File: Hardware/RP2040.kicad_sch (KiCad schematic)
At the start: 1 part, among them U1 RP2040

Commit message: Connect RP2040, STM32, temperature sensor
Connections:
- net SPI0_CS0: now reaches U1.3 (GPIO1)
- net SPI0_SCK: now reaches U1.4 (GPIO2)
- net SPI0_TX: now reaches U1.5 (GPIO3)
- net SPI0_RX: now reaches U1.6 (GPIO4)
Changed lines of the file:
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@@
 	(generator_version "9.0")
 	(paper "A3")
+	(wire
+		(pts
+			(xy 127 76.2) (xy 124.46 76.2)
+		)
+		(stroke
+			(width 0)
+			(type default)
+		)
+	)
+	(wire
+		(pts
+			(xy 127 78.74) (xy 124.46 78.74)
+		)
+		(stroke
+			(width 0)
+			(type default)
+		)
+	)
+	(wire
+		(pts
+			(xy 127 81.28) (xy 124.46 81.28)
+		)
+		(stroke
+			(width 0)
+			(type default)
+		)
+	)
+	(wire
+		(pts
+			(xy 127 73.66) (xy 124.46 73.66)
+		)
+		(stroke
+			(width 0)
+			(type default)
+		)
+	)
+	(hierarchical_label "SPI0_CS0"
+		(shape bidirectional)
+		(at 127 73.66 0)
+		(effects
+			(font
+				(size 1.27 1.27)
+			)
+			(justify left)
+		)
+	)
+	(hierarchical_label "SPI0_SCK"
+		(shape bidirectional)
+		(at 127 76.2 0)
+		(effects
+			(font
+				(size 1.27 1.27)
+			)
+			(justify left)
+		)
+	)
+	(hierarchical_label "SPI0_TX"
+		(shape bidirectional)
+		(at 127 78.74 0)
+		(effects
+			(font
+				(size 1.27 1.27)
+			)
+			(justify left)
+		)
+	)
+	(hierarchical_label "SPI0_RX"
+		(shape bidirectional)
+		(at 127 81.28 0)
+		(effects
+			(font
+				(size 1.27 1.27)
+			)
+			(justify left)
+		)
+	)
 	(symbol
 		(lib_id "MCU_RaspberryPi:RP2040")

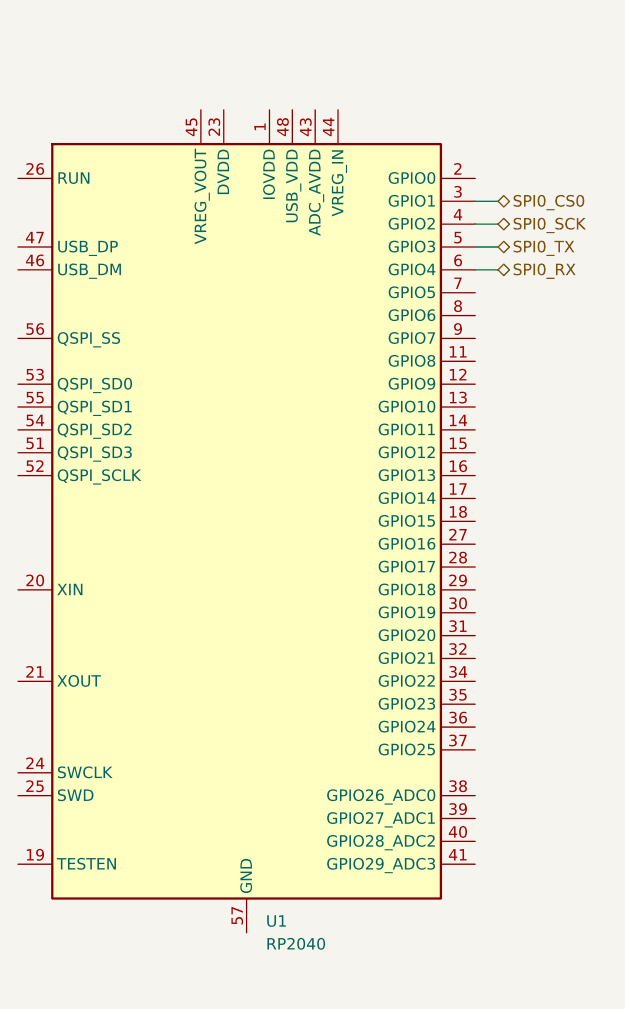
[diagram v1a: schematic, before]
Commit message: Assign SPI1 to Pi 4 <--> STM32
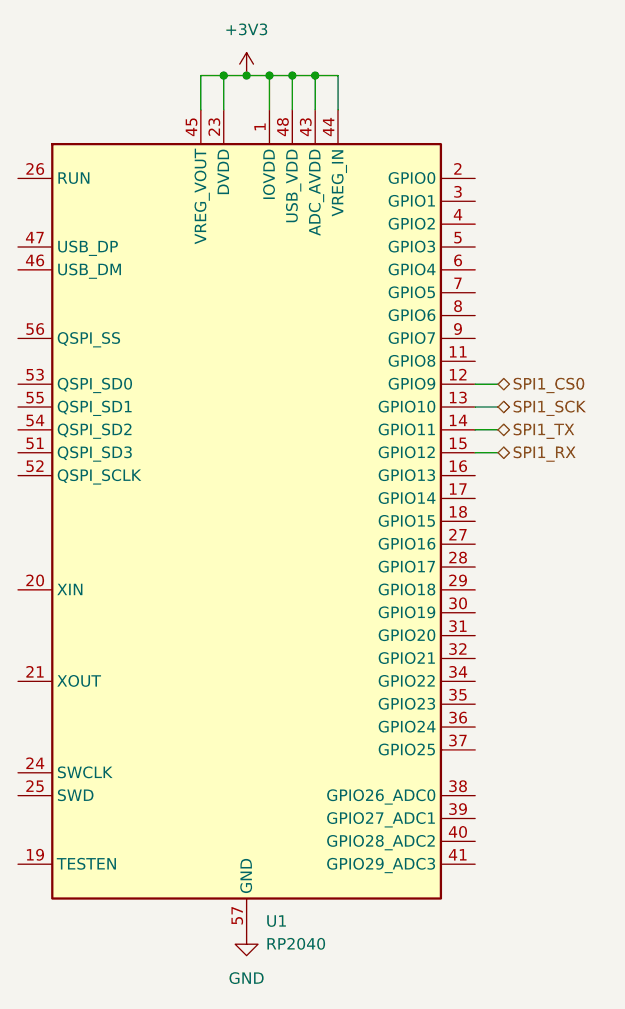
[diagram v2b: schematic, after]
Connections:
- net +3V3: now reaches U1.1 (IOVDD), U1.10 (IOVDD), U1.22 (IOVDD), U1.33 (IOVDD), U1.42 (IOVDD), U1.49 (IOVDD)
- net +3V3: now also U1.23 (DVDD), U1.43 (ADC_AVDD), U1.44 (VREG_IN), U1.45 (VREG_VOUT), U1.48 (USB_VDD), U1.50 (DVDD)
- net SPI1_CS0: now reaches U1.12 (GPIO9)
- net SPI1_SCK: now reaches U1.13 (GPIO10)
- net SPI1_TX: now reaches U1.14 (GPIO11)
- net SPI1_RX: now reaches U1.15 (GPIO12)
- net GND: now reaches U1.57 (GND)
- net SPI0_CS0: no longer names the net of U1.3 (GPIO1)
- net SPI0_RX: no longer names the net of U1.6 (GPIO4)
- net SPI0_SCK: no longer names the net of U1.4 (GPIO2)
- net SPI0_TX: no longer names the net of U1.5 (GPIO3)

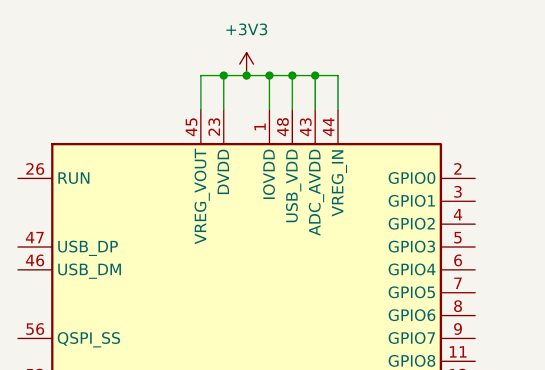
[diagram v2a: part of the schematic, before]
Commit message: Fix RP2040 1V1
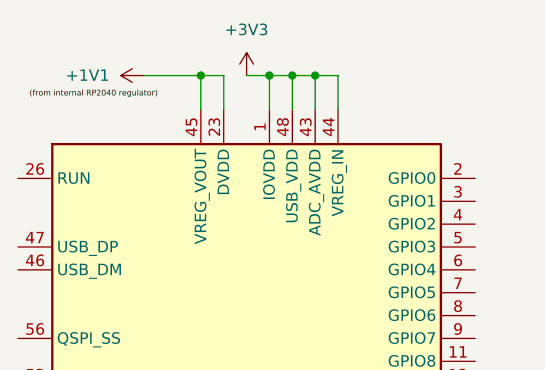
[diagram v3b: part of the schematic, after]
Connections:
- net +3V3: no longer U1.23 (DVDD), U1.45 (VREG_VOUT), U1.50 (DVDD)
- new net +1V1: U1.23 (DVDD), U1.45 (VREG_VOUT), U1.50 (DVDD)
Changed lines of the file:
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@@
 	(paper "A3")
-	(junction
-		(at 99.06 59.69)
-		(diameter 0)
-		(color 0 0 0 0)
-	)
 	(junction
 		(at 101.6 59.69)
@@
 	)
 	(junction
+		(at 93.98 59.69)
+		(diameter 0)
+		(color 0 0 0 0)
+	)
+	(junction
 		(at 104.14 59.69)
 		(diameter 0)
 		(color 0 0 0 0)
 	)
-	(junction
-		(at 96.52 59.69)
-		(diameter 0)
-		(color 0 0 0 0)
-	)
 	(wire
 		(pts
@@
 	(wire
 		(pts
-			(xy 93.98 59.69) (xy 96.52 59.69)
+			(xy 87.63 59.69) (xy 93.98 59.69)
 		)
 		(stroke
@@
 	(wire
 		(pts
-			(xy 96.52 59.69) (xy 96.52 63.5)
-		)
-		(stroke
-			(width 0)
-			(type default)
-		)
-	)
-	(wire
-		(pts
 			(xy 127 99.06) (xy 124.46 99.06)
 		)
@@
 	(wire
 		(pts
-			(xy 96.52 59.69) (xy 99.06 59.69)
-		)
-		(stroke
-			(width 0)
-			(type default)
-		)
-	)
-	(wire
-		(pts
 			(xy 127 101.6) (xy 124.46 101.6)
 		)
@@
 	(wire
 		(pts
+			(xy 96.52 63.5) (xy 96.52 59.69)
+		)
+		(stroke
+			(width 0)
+			(type default)
+		)
+	)
+	(wire
+		(pts
+			(xy 93.98 59.69) (xy 93.98 63.5)
+		)
+		(stroke
+			(width 0)
+			(type default)
+		)
+	)
+	(wire
+		(pts
 			(xy 127 93.98) (xy 124.46 93.98)
 		)
@@
 	(wire
 		(pts
+			(xy 96.52 59.69) (xy 93.98 59.69)
+		)
+		(stroke
+			(width 0)
+			(type default)
+		)
+	)
+	(wire
+		(pts
 			(xy 127 96.52) (xy 124.46 96.52)
 		)
@@
 	(wire
 		(pts
-			(xy 93.98 63.5) (xy 93.98 59.69)
-		)
-		(stroke
-			(width 0)
-			(type default)
-		)
-	)
-	(wire
-		(pts
 			(xy 104.14 59.69) (xy 106.68 59.69)
 		)
@@
 			(width 0)
 			(type default)
+		)
+	)
+	(label "(from internal RP2040 regulator)"
+		(at 74.93 62.23 0)
+		(effects
+			(font
+				(size 0.635 0.635)
+			)
+			(justify left bottom)
 		)
 	)
@@
 					(unit 1)
 				)
+			)
+		)
+	)
+	(symbol
+		(lib_id "power:+3V3")
+		(at 87.63 59.69 90)
+		(unit 1)
+		(exclude_from_sim no)
+		(in_bom yes)
+		(on_board yes)
+		(dnp no)
+		(fields_autoplaced yes)
+		(property "Reference" "#PWR030"
+			(at 91.44 59.69 0)
+			(effects
+				(font
+					(size 1.27 1.27)
+				)
+				(hide yes)
+			)
+		)
+		(property "Value" "+1V1"
+			(at 83.82 59.6899 90)
+			(effects
+				(font
+					(size 1.27 1.27)
+				)
+				(justify left)
+			)
+		)
+		(property "Footprint" ""
+			(at 87.63 59.69 0)
+			(effects
+				(font
+					(size 1.27 1.27)
+				)
+				(hide yes)
+			)
+		)
+		(property "Datasheet" ""
+			(at 87.63 59.69 0)
+			(effects
+				(font
+					(size 1.27 1.27)
+				)
+				(hide yes)
+			)
+		)
+		(property "Description" "Power symbol creates a global label with name \"+3V3\""
+			(at 87.63 59.69 0)
+			(effects
+				(font
+					(size 1.27 1.27)
+				)
+				(hide yes)
+			)
+		)
+		(pin "1"
+		)
+		(instances
+			(project "CTS-SAT-2-OBC-PCB"
+				(path "/58243925-df8d-4fc1-899e-fce866d1d25a/bec95c26-e44f-4f6a-97be-aee51e3bba5a"
+					(reference "#PWR030")
+					(unit 1)
+				)

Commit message: RP2040 Schematic
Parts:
- removed U1: RP2040, Package_DFN_QFN:QFN-56-1EP_7x7mm_P0.4mm_EP3.2x3.2mm, symbol MCU_RaspberryPi:RP2040
- added C1, C10, C11, C12, C13, C14, C4, C5, C7, C9: 100n, Capacitor_SMD:C_0402_1005Metric, symbol Device:C
- added C2, C3: 15p, Capacitor_SMD:C_0402_1005Metric, symbol Device:C
- added C6, C8: 1u, Capacitor_SMD:C_0402_1005Metric, symbol Device:C
- added R1: NP, Resistor_SMD:R_0402_1005Metric, symbol Device:R_US
- added R2, R3: 1k, Resistor_SMD:R_0402_1005Metric, symbol Device:R_US
- added R4, R5: 27, Resistor_SMD:R_0402_1005Metric, symbol Device:R_US
- added U1: W25Q128JVS, Package_SO:SOIC-8_5.23x5.23mm_P1.27mm, symbol Memory_Flash:W25Q128JVS
- added U2: RP2040, RP2040:RP2040-QFN-56, symbol RP2040:RP2040
- added Y1: ABM8-272-T3, Crystal:Crystal_SMD_3225-4Pin_3.2x2.5mm, symbol Device:Crystal_GND24
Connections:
- net +1V1: now also C4.1, C5.1, C6.1, U2.23 (DVDD), U2.45 (VREG_VOUT), U2.50 (DVDD)
- net +3V3: now also C1.1, C10.1, C11.1, C12.1, C13.1, C14.1, C7.1, C8.1, C9.1, R1.2, U1.8 (VCC), U2.1 (IOVDD), U2.10 (IOVDD), U2.22 (IOVDD), U2.33 (IOVDD), U2.42 (IOVDD), U2.43 (ADC_AVDD), U2.44 (VREG_IN), U2.48 (USB_VDD), U2.49 (IOVDD)
- net GND: now also C1.2, C10.2, C11.2, C12.2, C13.2, C14.2, C2.2, C3.2, C4.2, C5.2, C6.2, C7.2, C8.2, C9.2, U1.4 (GND), U2.19 (TESTEN), U2.57 (GND), Y1.2, Y1.4
- net SPI1_CS0: now also U2.12 (GPIO9)
- net SPI1_RX: now also U2.15 (GPIO12)
- net SPI1_SCK: now also U2.13 (GPIO10)
- net SPI1_TX: now also U2.14 (GPIO11)
- new net: C2.1, U2.20 (XIN), Y1.1
- new net: R3.1, U2.21 (XOUT)
- new net: R5.2, U2.46 (USB_DM)
- new net: R4.2, U2.47 (USB_DP)
- new net: U1.7 (IO3), U2.51 (QSPI_SD3)
- new net: U1.6 (CLK), U2.52 (QSPI_SCLK)
- new net: U1.5 (DI(IO0)), U2.53 (QSPI_SD0)
- new net: U1.3 (IO2), U2.54 (QSPI_SD2)
- new net: U1.2 (DO(IO1)), U2.55 (QSPI_SD1)
- new net: R1.1, R2.1, U1.1 (~{CS}), U2.56 (QSPI_SS)
- new net: C3.1, R3.2, Y1.3
- new net RUN: U2.26 (RUN)
- new net SWCLK: U2.24 (SWCLK)
- new net SWD: U2.25 (SWD)
- new net USB_D+: R4.1
- new net USB_D-: R5.1
- new net ~{BOOTSEL}: R2.2
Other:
- note added: "(from internal RP2040 regulator)"
- note added: "Crystal"
- note added: "Flash"
- note added: "Make sure C6 is close to pin 45 of RP2040"
- note added: "Make sure C8 is close to pin 44 of RP2040"
- note added: "Make sure R4 and R5 are close to RP2040"
- note added: "Some other chips may need R1 = 10k"

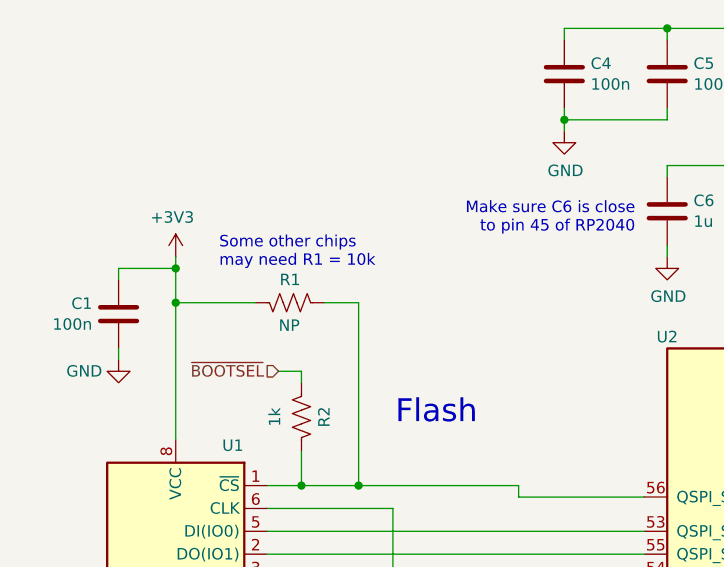
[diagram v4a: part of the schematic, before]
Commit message: Add fast clock
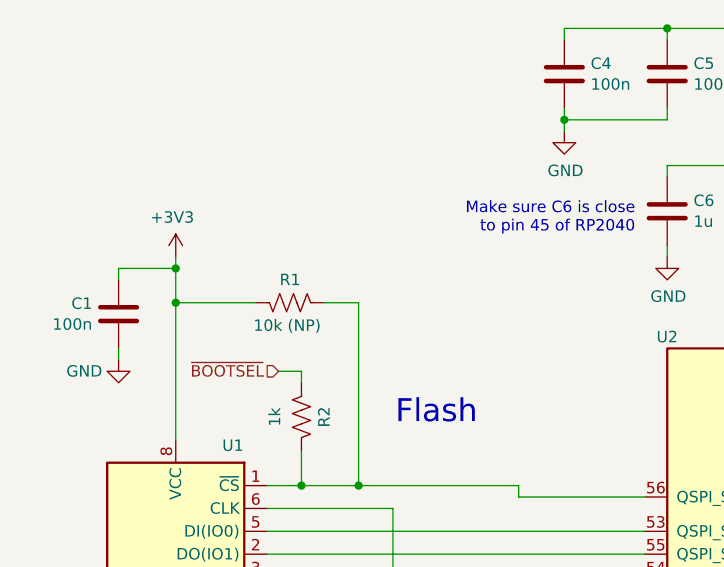
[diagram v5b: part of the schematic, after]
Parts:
- R1: value NP -> 10k (NP)
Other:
- note removed: "Some other chips may need R1 = 10k"
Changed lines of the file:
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@@
 		)
 	)
-	(text "Some other chips \nmay need R1 = 10k"
-		(exclude_from_sim no)
-		(at 128.016 88.9 0)
-		(effects
-			(font
-				(size 1.27 1.27)
-			)
-			(justify left bottom)
-		)
-	)
 	(text "(from internal RP2040 regulator)"
 		(exclude_from_sim no)
@@
 			)
 		)
-		(property "Value" "NP"
-			(at 134.62 95.25 90)
+		(property "Value" "10k (NP)"
+			(at 131.826 95.25 90)
 			(effects
 				(font

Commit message: Connect connectors
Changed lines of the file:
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@@
 		(on_board yes)
 		(dnp no)
-		(property "Reference" "#PWR06"
+		(property "Reference" "#PWR6"
 			(at 123.19 154.94 0)
 			(effects
@@
 		)
 		(property "Value" "GND"
-			(at 119.38 149.86 0)
+			(at 123.19 152.4 0)
 			(effects
 				(font
@@
 			)
 		)
-		(property "Description" ""
+		(property "Description" "Power symbol creates a global label with name \"GND\" , ground"
 			(at 123.19 148.59 0)
 			(effects
@@
 					(size 1.27 1.27)
 				)
-			)
-		)
-		(pin "1"
-		)
-		(instances
-			(project "CTS-SAT-2-OBC-PCB"
-				(path "/58243925-df8d-4fc1-899e-fce866d1d25a/bec95c26-e44f-4f6a-97be-aee51e3bba5a"
-					(reference "#PWR06")
+				(hide yes)
+			)
+		)
+		(pin "1"
+		)
+		(instances
+			(project "CTS-SAT-2-OBC-PCB"
+				(path "/58243925-df8d-4fc1-899e-fce866d1d25a/bec95c26-e44f-4f6a-97be-aee51e3bba5a"
+					(reference "#PWR6")
 					(unit 1)
 				)
@@
 		(on_board yes)
 		(dnp no)
-		(property "Reference" "#PWR012"
+		(property "Reference" "#PWR12"
 			(at 207.01 205.74 0)
 			(effects
@@
 		)
 		(property "Value" "GND"
-			(at 207.137 203.7842 0)
+			(at 207.01 203.2 0)
 			(effects
 				(font
@@
 			)
 		)
-		(property "Description" ""
+		(property "Description" "Power symbol creates a global label with name \"GND\" , ground"
 			(at 207.01 199.39 0)
 			(effects
@@
 					(size 1.27 1.27)
 				)
-			)
-		)
-		(pin "1"
-		)
-		(instances
-			(project "CTS-SAT-2-OBC-PCB"
-				(path "/58243925-df8d-4fc1-899e-fce866d1d25a/bec95c26-e44f-4f6a-97be-aee51e3bba5a"
-					(reference "#PWR012")
+				(hide yes)
+			)
+		)
+		(pin "1"
+		)
+		(instances
+			(project "CTS-SAT-2-OBC-PCB"
+				(path "/58243925-df8d-4fc1-899e-fce866d1d25a/bec95c26-e44f-4f6a-97be-aee51e3bba5a"
+					(reference "#PWR12")
 					(unit 1)
 				)
@@
 		(on_board yes)
 		(dnp no)
-		(property "Reference" "#PWR01"
+		(property "Reference" "#PWR1"
 			(at 116.84 105.41 0)
 			(effects
@@
 		)
 		(property "Value" "GND"
-			(at 113.03 100.33 0)
+			(at 116.84 102.87 0)
 			(effects
 				(font
@@
 			)
 		)
-		(property "Description" ""
+		(property "Description" "Power symbol creates a global label with name \"GND\" , ground"
 			(at 116.84 99.06 0)
 			(effects
@@
 					(size 1.27 1.27)
 				)
-			)
-		)
-		(pin "1"
-		)
-		(instances
-			(project "CTS-SAT-2-OBC-PCB"
-				(path "/58243925-df8d-4fc1-899e-fce866d1d25a/bec95c26-e44f-4f6a-97be-aee51e3bba5a"
-					(reference "#PWR01")
+				(hide yes)
+			)
+		)
+		(pin "1"
+		)
+		(instances
+			(project "CTS-SAT-2-OBC-PCB"
+				(path "/58243925-df8d-4fc1-899e-fce866d1d25a/bec95c26-e44f-4f6a-97be-aee51e3bba5a"
+					(reference "#PWR1")
 					(unit 1)
 				)
@@
 		(on_board yes)
 		(dnp no)
-		(property "Reference" "#PWR015"
+		(property "Reference" "#PWR15"
 			(at 300.99 81.28 0)
 			(effects
@@
 		)
 		(property "Value" "GND"
-			(at 301.117 79.3242 0)
+			(at 300.99 78.74 0)
 			(effects
 				(font
@@
 			)
 		)
-		(property "Description" ""
+		(property "Description" "Power symbol creates a global label with name \"GND\" , ground"
 			(at 300.99 74.93 0)
 			(effects
@@
 					(size 1.27 1.27)
 				)
-			)
-		)
-		(pin "1"
-		)
-		(instances
-			(project "CTS-SAT-2-OBC-PCB"
-				(path "/58243925-df8d-4fc1-899e-fce866d1d25a/bec95c26-e44f-4f6a-97be-aee51e3bba5a"
-					(reference "#PWR015")
+				(hide yes)
+			)
+		)
+		(pin "1"
+		)
+		(instances
+			(project "CTS-SAT-2-OBC-PCB"
+				(path "/58243925-df8d-4fc1-899e-fce866d1d25a/bec95c26-e44f-4f6a-97be-aee51e3bba5a"
+					(reference "#PWR15")
 					(unit 1)
 				)
@@
 		(on_board yes)
 		(dnp no)
-		(property "Reference" "#PWR07"
+		(property "Reference" "#PWR7"
 			(at 135.89 154.94 0)
 			(effects
@@
 		)
 		(property "Value" "GND"
-			(at 139.7 149.86 0)
+			(at 135.89 152.4 0)
 			(effects
 				(font
@@
 			)
 		)
-		(property "Description" ""
+		(property "Description" "Power symbol creates a global label with name \"GND\" , ground"
 			(at 135.89 148.59 0)
 			(effects
@@
 					(size 1.27 1.27)
 				)
-			)
-		)
-		(pin "1"
-		)
-		(instances
-			(project "CTS-SAT-2-OBC-PCB"
-				(path "/58243925-df8d-4fc1-899e-fce866d1d25a/bec95c26-e44f-4f6a-97be-aee51e3bba5a"
-					(reference "#PWR07")
+				(hide yes)
+			)
+		)
+		(pin "1"
+		)
+		(instances
+			(project "CTS-SAT-2-OBC-PCB"
+				(path "/58243925-df8d-4fc1-899e-fce866d1d25a/bec95c26-e44f-4f6a-97be-aee51e3bba5a"
+					(reference "#PWR7")
 					(unit 1)
 				)
@@
 		(on_board yes)
 		(dnp no)
-		(property "Reference" "#PWR011"
+		(property "Reference" "#PWR11"
 			(at 194.31 205.74 0)
 			(effects
@@
 		)
 		(property "Value" "GND"
-			(at 194.437 203.7842 0)
+			(at 194.31 203.2 0)
 			(effects
 				(font
@@
 			)
 		)
-		(property "Description" ""
+		(property "Description" "Power symbol creates a global label with name \"GND\" , ground"
 			(at 194.31 199.39 0)
 			(effects
@@
 					(size 1.27 1.27)
 				)
-			)
-		)
-		(pin "1"
-		)
-		(instances
-			(project "CTS-SAT-2-OBC-PCB"
-				(path "/58243925-df8d-4fc1-899e-fce866d1d25a/bec95c26-e44f-4f6a-97be-aee51e3bba5a"
-					(reference "#PWR011")
+				(hide yes)
+			)
+		)
+		(pin "1"
+		)
+		(instances
+			(project "CTS-SAT-2-OBC-PCB"
+				(path "/58243925-df8d-4fc1-899e-fce866d1d25a/bec95c26-e44f-4f6a-97be-aee51e3bba5a"
+					(reference "#PWR11")
 					(unit 1)
 				)
@@
 		(on_board yes)
 		(dnp no)
-		(property "Reference" "#PWR05"
+		(property "Reference" "#PWR5"
 			(at 107.95 162.56 0)
 			(effects
@@
 		)
 		(property "Value" "GND"
-			(at 108.077 160.6042 0)
+			(at 107.95 160.02 0)
 			(effects
 				(font
@@
 			)
 		)
-		(property "Description" ""
+		(property "Description" "Power symbol creates a global label with name \"GND\" , ground"
 			(at 107.95 156.21 0)
 			(effects
@@
 					(size 1.27 1.27)
 				)
-			)
-		)
-		(pin "1"
-		)
-		(instances
-			(project "CTS-SAT-2-OBC-PCB"
-				(path "/58243925-df8d-4fc1-899e-fce866d1d25a/bec95c26-e44f-4f6a-97be-aee51e3bba5a"
-					(reference "#PWR05")
+				(hide yes)
+			)
+		)
+		(pin "1"
+		)
+		(instances
+			(project "CTS-SAT-2-OBC-PCB"
+				(path "/58243925-df8d-4fc1-899e-fce866d1d25a/bec95c26-e44f-4f6a-97be-aee51e3bba5a"
+					(reference "#PWR5")
 					(unit 1)
 				)
@@
 		(on_board yes)
 		(dnp no)
-		(property "Reference" "#PWR09"
+		(property "Reference" "#PWR9"
 			(at 177.8 93.98 0)
 			(effects
@@
 		)
 		(property "Value" "GND"
-			(at 177.927 92.0242 0)
+			(at 177.8 91.44 0)
 			(effects
 				(font
@@
 			)
 		)
-		(property "Description" ""
+		(property "Description" "Power symbol creates a global label with name \"GND\" , ground"
 			(at 177.8 87.63 0)
 			(effects
@@
 					(size 1.27 1.27)
 				)
-			)
-		)
-		(pin "1"
-		)
-		(instances
-			(project "CTS-SAT-2-OBC-PCB"
-				(path "/58243925-df8d-4fc1-899e-fce866d1d25a/bec95c26-e44f-4f6a-97be-aee51e3bba5a"
-					(reference "#PWR09")
+				(hide yes)
+			)
+		)
+		(pin "1"
+		)
+		(instances
+			(project "CTS-SAT-2-OBC-PCB"
+				(path "/58243925-df8d-4fc1-899e-fce866d1d25a/bec95c26-e44f-4f6a-97be-aee51e3bba5a"
+					(reference "#PWR9")
 					(unit 1)
 				)
@@
 		(on_board yes)
 		(dnp no)
-		(property "Reference" "#PWR08"
+		(property "Reference" "#PWR8"
 			(at 166.37 80.01 0)
 			(effects
@@
 		)
 		(property "Value" "GND"
-			(at 166.497 78.0542 0)
+			(at 166.37 77.47 0)
 			(effects
 				(font
@@
 			)
 		)
-		(property "Description" ""
+		(property "Description" "Power symbol creates a global label with name \"GND\" , ground"
 			(at 166.37 73.66 0)
 			(effects
@@
 					(size 1.27 1.27)
 				)
-			)
-		)
-		(pin "1"
-		)
-		(instances
-			(project "CTS-SAT-2-OBC-PCB"
-				(path "/58243925-df8d-4fc1-899e-fce866d1d25a/bec95c26-e44f-4f6a-97be-aee51e3bba5a"
-					(reference "#PWR08")
+				(hide yes)
+			)
+		)
+		(pin "1"
+		)
+		(instances
+			(project "CTS-SAT-2-OBC-PCB"
+				(path "/58243925-df8d-4fc1-899e-fce866d1d25a/bec95c26-e44f-4f6a-97be-aee51e3bba5a"
+					(reference "#PWR8")
 					(unit 1)
 				)
@@
 		(on_board yes)
 		(dnp no)
-		(property "Reference" "#PWR014"
+		(property "Reference" "#PWR14"
 			(at 232.41 93.98 0)
 			(effects
@@
 		)
 		(property "Value" "GND"
-			(at 232.537 92.0242 0)
+			(at 232.41 91.44 0)
 			(effects
 				(font
@@
 			)
 		)
-		(property "Description" ""
+		(property "Description" "Power symbol creates a global label with name \"GND\" , ground"
 			(at 232.41 87.63 0)
 			(effects
@@
 					(size 1.27 1.27)
 				)
-			)
-		)
-		(pin "1"
-		)
-		(instances
-			(project "CTS-SAT-2-OBC-PCB"
-				(path "/58243925-df8d-4fc1-899e-fce866d1d25a/bec95c26-e44f-4f6a-97be-aee51e3bba5a"
-					(reference "#PWR014")
+				(hide yes)
+			)
+		)
+		(pin "1"
+		)
+		(instances
+			(project "CTS-SAT-2-OBC-PCB"
+				(path "/58243925-df8d-4fc1-899e-fce866d1d25a/bec95c26-e44f-4f6a-97be-aee51e3bba5a"
+					(reference "#PWR14")
 					(unit 1)
 				)
@@
 		(on_board yes)
 		(dnp no)
-		(property "Reference" "#PWR03"
+		(property "Reference" "#PWR3"
 			(at 123.19 140.335 0)
 			(effects
@@
 		)
 		(property "Value" "GND"
-			(at 127 135.255 0)
+			(at 123.19 137.795 0)
 			(effects
 				(font
@@
 			)
 		)
-		(property "Description" ""
+		(property "Description" "Power symbol creates a global label with name \"GND\" , ground"
 			(at 123.19 133.985 0)
 			(effects
@@
 					(size 1.27 1.27)
 				)
-			)
-		)
-		(pin "1"
-		)
-		(instances
-			(project "CTS-SAT-2-OBC-PCB"
-				(path "/58243925-df8d-4fc1-899e-fce866d1d25a/bec95c26-e44f-4f6a-97be-aee51e3bba5a"
-					(reference "#PWR03")
-					(unit 1)
-				)
+				(hide yes)
+			)
+		)
+		(pin "1"
+		)
+		(instances
+			(project "CTS-SAT-2-OBC-PCB"
+				(path "/58243925-df8d-4fc1-899e-fce866d1d25a/bec95c26-e44f-4f6a-97be-aee51e3bba5a"
+					(reference "#PWR3")
+					(unit 1)
+				)
